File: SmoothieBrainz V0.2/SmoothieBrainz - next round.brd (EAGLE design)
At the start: 100 x 80 mm, 122 parts, among them IC1 LPC1769, IC5 LD117ADT33TR, Q1 BSL207SP, Q2 12MHz, SW1 SW_TACT_4P_B, SW3 SW_TACT_4P_B, U2 HC_05, U3 USD-SOCKETUSD, X14 USBPTH

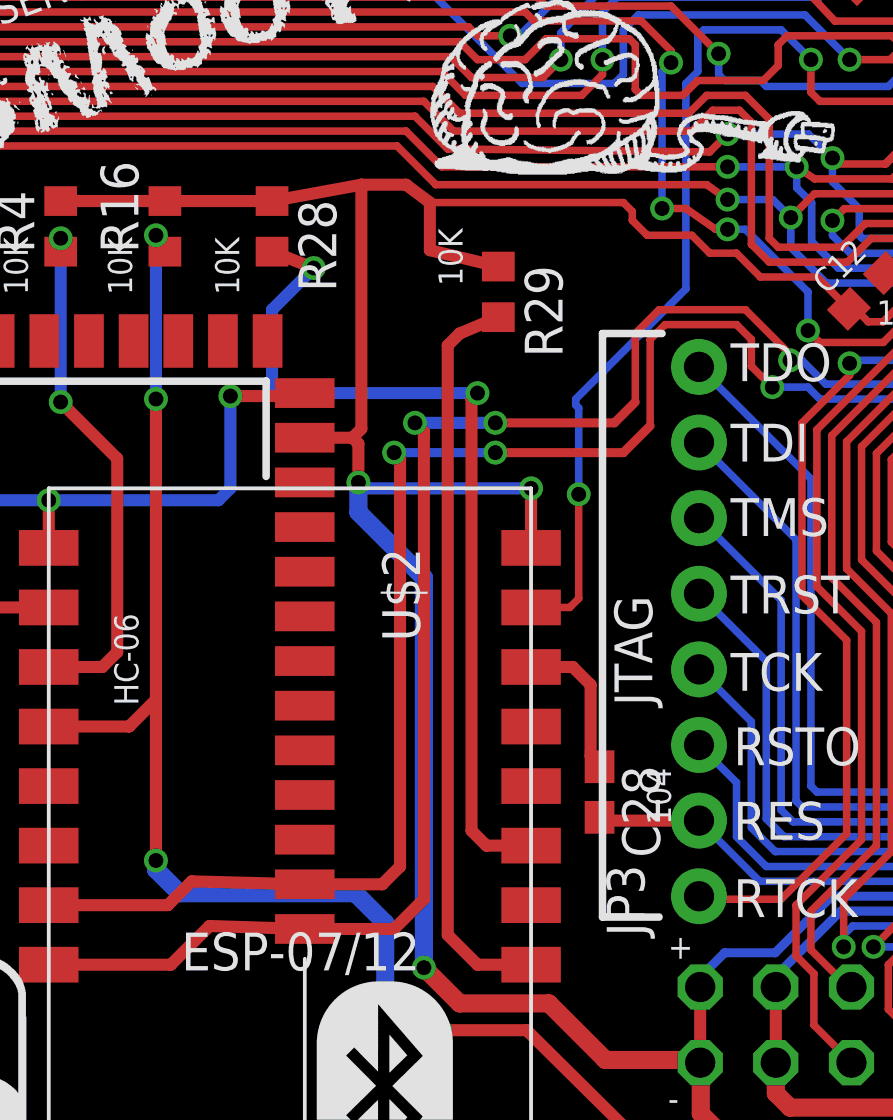
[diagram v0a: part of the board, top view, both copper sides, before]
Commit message: Minor routing cleanup
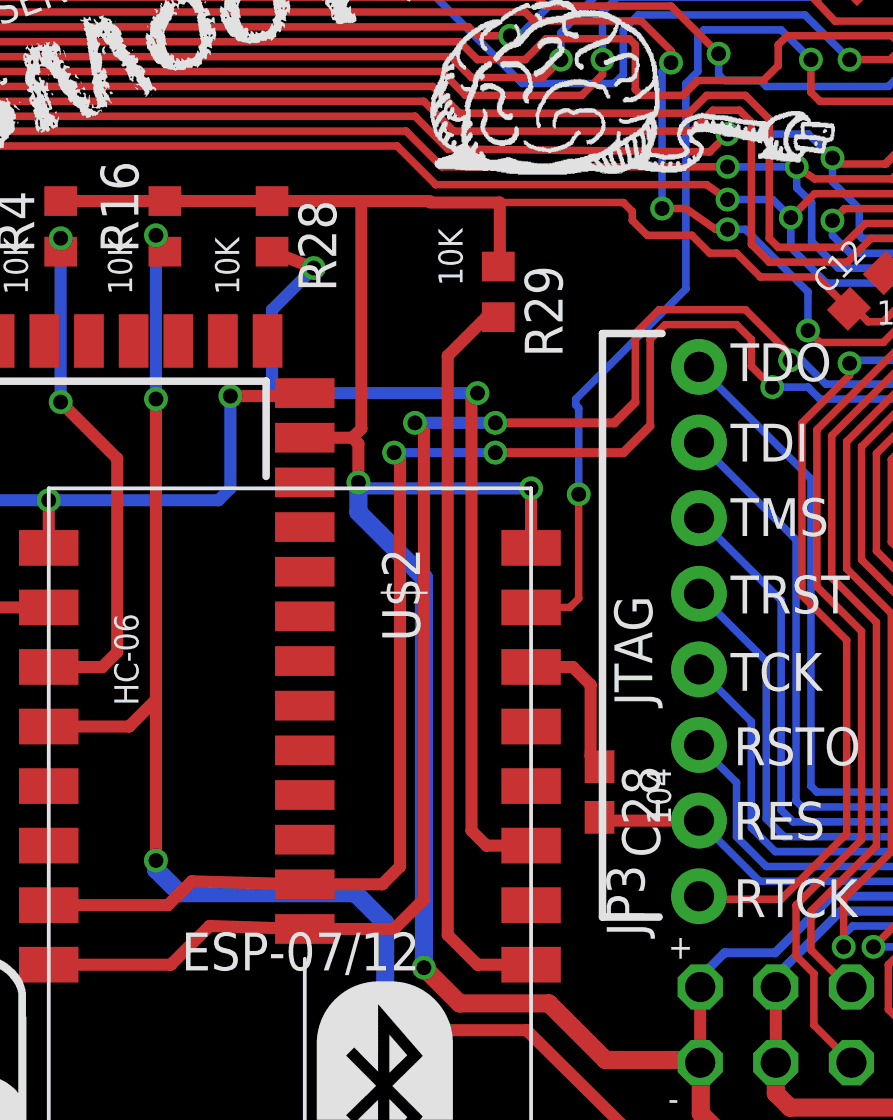
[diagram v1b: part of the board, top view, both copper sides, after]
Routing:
- net 3.3V: track 542.7 -> 540.1 mm
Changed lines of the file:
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@@
 <wire x1="60.35" y1="64.9" x2="61.8" y2="64.9" width="0.8128" layer="1"/>
 <wire x1="61.8" y1="64.9" x2="62" y2="65.1" width="0.8128" layer="1"/>
+<wire x1="59.85" y1="65" x2="60.25" y2="65" width="0.8128" layer="1"/>
+<wire x1="60.25" y1="65" x2="60.35" y2="64.9" width="0.8128" layer="1"/>
 <wire x1="92.9" y1="67.7" x2="92.6" y2="67.8" width="0" layer="19" extent="16-16"/>
 <wire x1="75.9" y1="57.2" x2="76.577" y2="57.225" width="0" layer="19" extent="1-1"/>
@@
 <wire x1="10.2" y1="36.1" x2="10.2" y2="43.7" width="0" layer="19" extent="1-1"/>
 <wire x1="10.3" y1="23.4" x2="10.3" y2="23.8" width="0" layer="19" extent="16-16"/>
-<wire x1="59.85" y1="65" x2="60.25" y2="65" width="0.8128" layer="1"/>
-<wire x1="60.25" y1="65" x2="60.35" y2="64.9" width="0.8128" layer="1"/>
 </signal>
 <signal name="3.3V">
@@
 <contactref element="R16" pad="2"/>
 <contactref element="U2" pad="12"/>
-<wire x1="30.5" y1="34.4" x2="31.3" y2="33.8" width="0.4064" layer="1"/>
-<wire x1="31.3" y1="33.8" x2="37.8" y2="33.8" width="0.254" layer="1"/>
+<wire x1="31.3" y1="33.8" x2="33.65" y2="33.8" width="0.4064" layer="1"/>
+<wire x1="33.65" y1="33.8" x2="37.8" y2="33.8" width="0.254" layer="1"/>
 <wire x1="37.8" y1="33.8" x2="38.1" y2="33.5" width="0.254" layer="1"/>
 <wire x1="38.1" y1="33.5" x2="38.1" y2="33.2" width="0.254" layer="1"/>
@@
 <wire x1="27.1" y1="25.9" x2="28.7" y2="25.9" width="0.4064" layer="1"/>
 <wire x1="28.7" y1="25.9" x2="29" y2="26.2" width="0.4064" layer="1"/>
-<wire x1="29" y1="26.2" x2="29" y2="34.4" width="0.4064" layer="1"/>
-<wire x1="29" y1="34.4" x2="26" y2="33.85" width="0.4064" layer="1"/>
-<wire x1="30.5" y1="34.4" x2="29" y2="34.4" width="0.4064" layer="1"/>
-<wire x1="33.6" y1="31.65" x2="31.3" y2="32.2" width="0.4064" layer="1"/>
-<wire x1="31.3" y1="32.2" x2="31.3" y2="33.8" width="0.4064" layer="1"/>
+<wire x1="29" y1="26.2" x2="29" y2="33.85" width="0.4064" layer="1"/>
+<wire x1="29" y1="33.85" x2="26" y2="33.85" width="0.4064" layer="1"/>
 <wire x1="34.7" y1="22.2" x2="34.7" y2="24.2" width="0.4064" layer="1"/>
 <via x="34.7" y="24.2" extent="1-16" drill="0.5"/>
@@
 <wire x1="79" y1="67.4825" x2="78.3825" y2="68.1" width="0.254" layer="1"/>
 <wire x1="78.3825" y1="68.1" x2="77.4" y2="68.1" width="0.254" layer="1"/>
+<wire x1="29" y1="33.85" x2="31.3" y2="33.85" width="0.4064" layer="1"/>
+<wire x1="31.3" y1="33.85" x2="31.3" y2="33.8" width="0.254" layer="1"/>
+<wire x1="33.6" y1="31.65" x2="33.65" y2="31.65" width="0.254" layer="1"/>
+<wire x1="33.65" y1="31.65" x2="33.65" y2="33.8" width="0.4064" layer="1"/>
 </signal>
 <signal name="AVCC">
@@
 <wire x1="34.7" y1="8.2" x2="32.9" y2="8.2" width="0.4064" layer="1"/>
 <wire x1="32.9" y1="8.2" x2="31.9" y2="9.2" width="0.4064" layer="1"/>
-<wire x1="32.3" y1="29.4" x2="33.6" y2="29.95" width="0.4064" layer="1"/>
-<wire x1="31.9" y1="9.2" x2="31.9" y2="29" width="0.4064" layer="1"/>
-<wire x1="31.9" y1="29" x2="32.3" y2="29.4" width="0.4064" layer="1"/>
+<wire x1="31.9" y1="9.2" x2="31.9" y2="28.65" width="0.4064" layer="1"/>
+<wire x1="33.6" y1="29.95" x2="33.2" y2="29.95" width="0.4064" layer="1"/>
+<wire x1="33.2" y1="29.95" x2="31.9" y2="28.65" width="0.4064" layer="1"/>
 </signal>
 <signal name="N$18">
